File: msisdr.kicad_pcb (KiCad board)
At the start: 2 copper layers, 95.9 x 91.1 mm, 72 parts, among them J1 SMA_UHF, J2 Raspberry_Pi_2_3, J3 USB_OTG, U1 msi2500, U2 B39431B3710U410, U3 msi001, U4 RT9193-28, U5 AP7313-33SAG, U6 PGA-103, Y1 24MHZ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

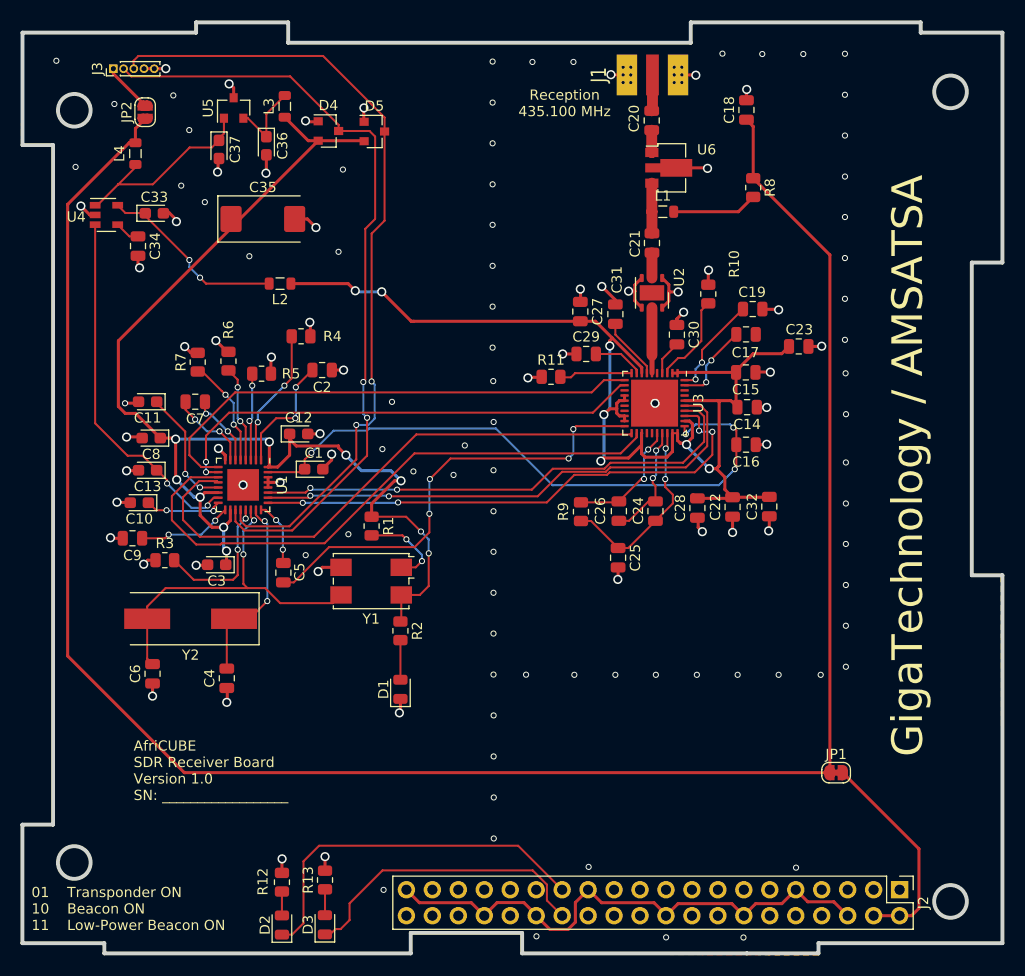
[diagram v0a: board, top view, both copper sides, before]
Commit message: adding v2 2 filter front end filter
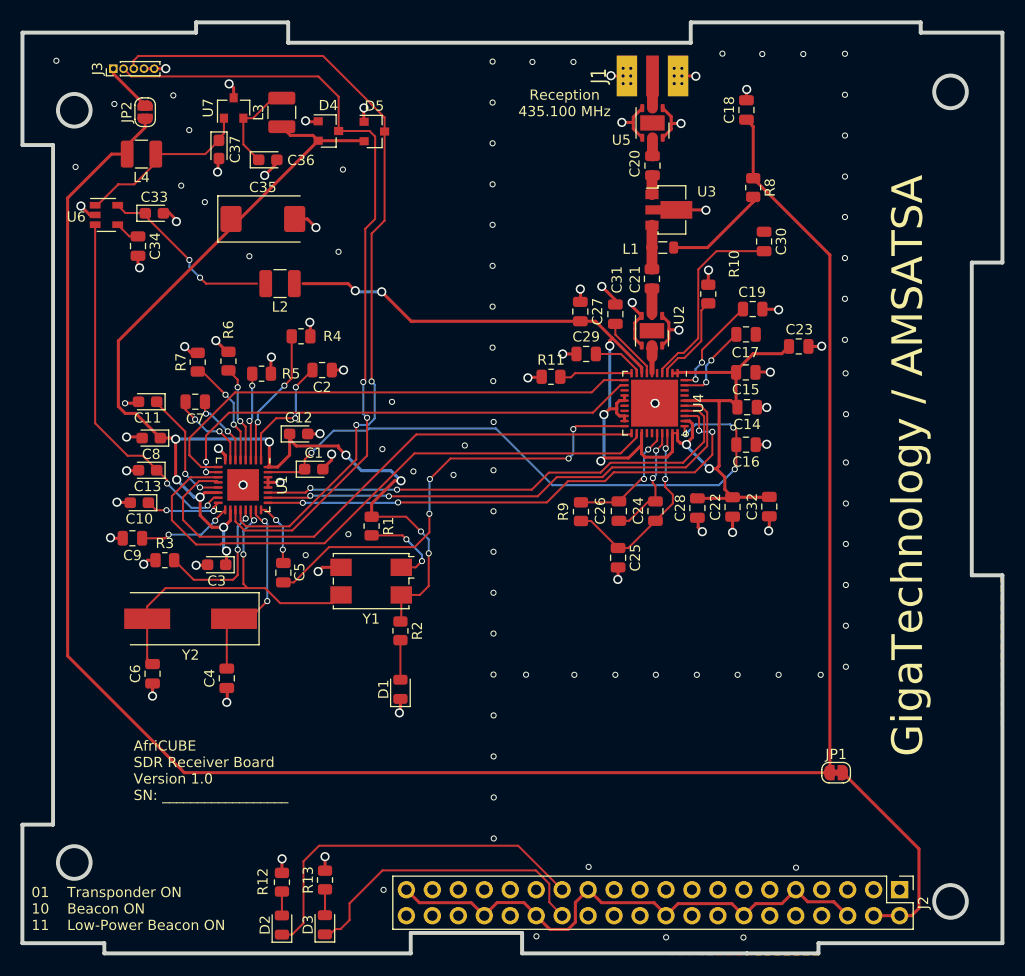
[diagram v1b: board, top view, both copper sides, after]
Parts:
- added U5: B39431B3710U410, Package_DFN_QFN:DFN-6-1EP_3x3mm_P1mm_EP1.5x2.4mm, F.Cu at (142.5, 66.5)
- L2, L3, L4: value L -> 15uH; footprint Inductor_SMD:L_0805_2012Metric -> Inductor_SMD:L_1210_3225Metric
- moved C30 12.5 mm to (153.5, 78.1)
- moved C20 4.42 mm to (142.5, 70.7)
- moved U3 4.11 mm to (144.1, 75.0)
- moved U2 3.71 mm to (142.5, 86.8)
- moved L1 3.51 mm to (143.6, 78.7)
- moved C21 3.51 mm to (142.5, 81.8)
- moved C36 1.38 mm to (104.9, 70.1), turned to 0 degrees
- moved L3 0.66 mm to (106.3, 65.5)
- moved L4 0.60 mm to (92.5, 69.5), turned to 180 degrees
- moved J1 0.10 mm to (142.5, 59.4)
- renumbered U6 to U3, U3 to U4, U4 to U6, U5 to U7
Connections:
- C20 pad 1: UHF_AMP -> Net-(C20-Pad1)
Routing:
- net Net-(C30-Pad2): track 3.41 -> 19.1 mm
- net GND: track 140.0 -> 149.1 mm, vias 127 -> 128
- net UHF_400_1000MHZ_Filter: track 6.25 -> 2.69 mm
- net Net-(C37-Pad1): track 19.7 -> 17.5 mm
- net Net-(C20-Pad1): track 0.00 -> 1.78 mm
- net Net-(L1-Pad2): track 8.67 -> 10.4 mm
- net USB_DP: track 77.0 -> 78.6 mm
- net Net-(C36-Pad1): track 7.78 -> 9.27 mm
- net VRF: track 116.7 -> 115.5 mm
- net Net-(C33-Pad1): track 18.3 -> 17.2 mm
- net Net-(C21-Pad1): track 4.91 -> 4.31 mm
- net +5V: track 202.6 -> 203.2 mm
